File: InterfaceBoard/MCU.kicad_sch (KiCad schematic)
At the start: 1 part, among them J1 Conn_ARM_JTAG_SWD_10

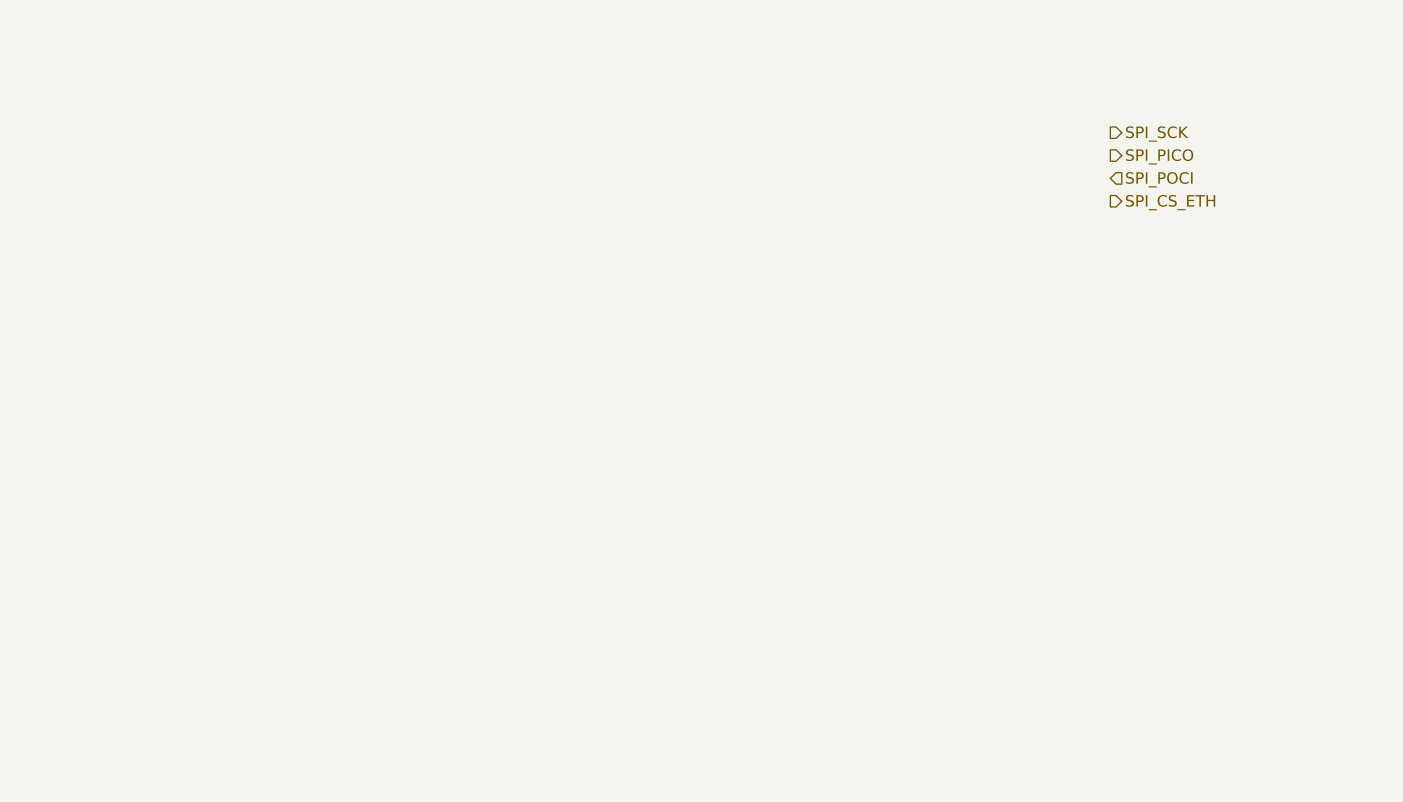
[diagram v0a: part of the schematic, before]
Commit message: InterfaceBoard: Add RS-232/DE-9
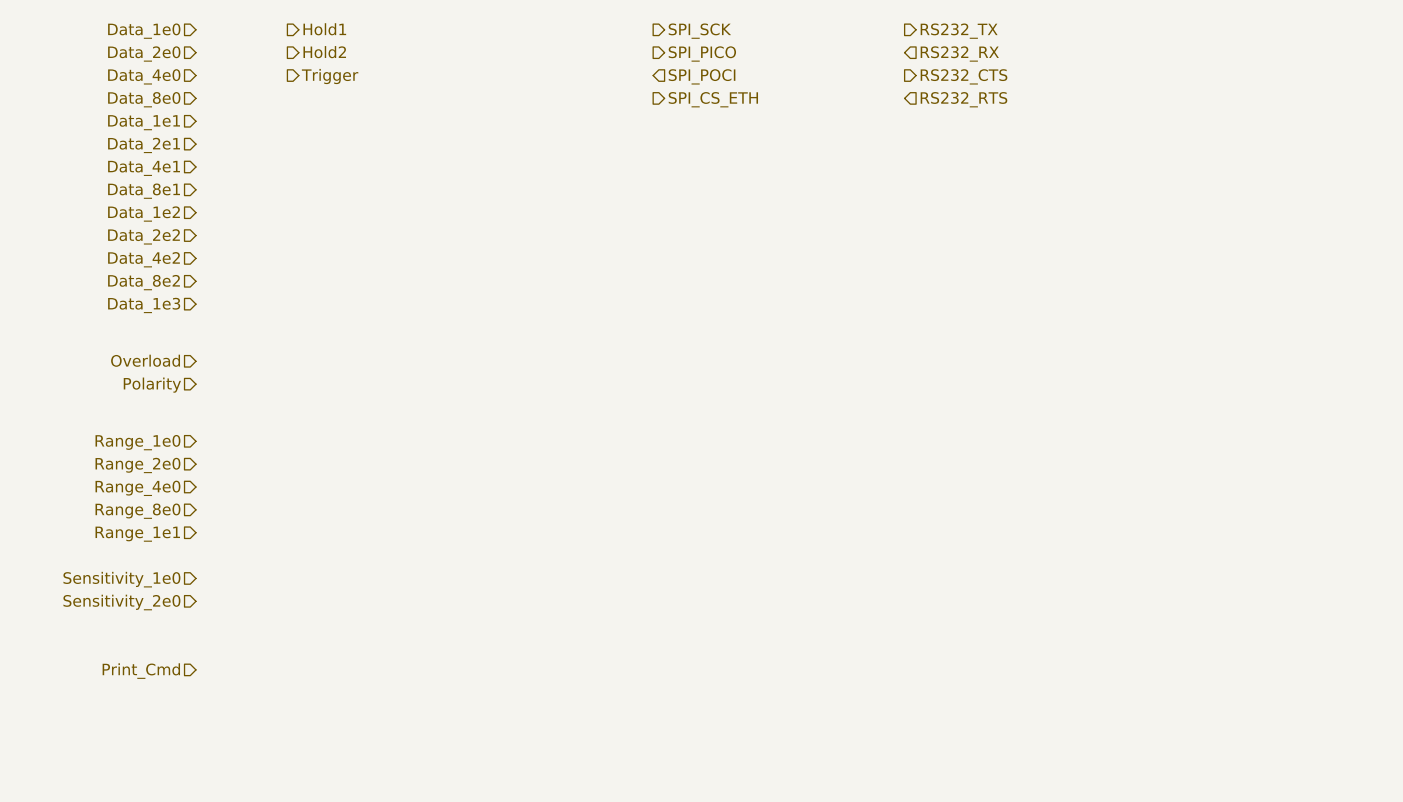
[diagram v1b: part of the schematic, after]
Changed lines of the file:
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@@
 (kicad_sch (version 20211123) (generator eeschema)
   (paper "A4")
-  (hierarchical_label "SPI_POCI" (shape input) (at 137.16 34.29 0)
+  (hierarchical_label "Data_2e0" (shape input) (at 35.56 20.32 180)
+    (effects (font (size 1.27 1.27)) (justify right))
+  )
+  (hierarchical_label "Hold1" (shape output) (at 45.72 17.78 0)
     (effects (font (size 1.27 1.27)) (justify left))
   )
-  (hierarchical_label "SPI_PICO" (shape output) (at 137.16 31.75 0)
+  (hierarchical_label "RS232_RTS" (shape input) (at 114.3 25.4 0)
     (effects (font (size 1.27 1.27)) (justify left))
   )
-  (hierarchical_label "SPI_CS_ETH" (shape output) (at 137.16 36.83 0)
+  (hierarchical_label "Range_4e0" (shape input) (at 35.56 68.58 180)
+    (effects (font (size 1.27 1.27)) (justify right))
+  )
+  (hierarchical_label "Data_1e1" (shape input) (at 35.56 27.94 180)
+    (effects (font (size 1.27 1.27)) (justify right))
+  )
+  (hierarchical_label "RS232_TX" (shape output) (at 114.3 17.78 0)
     (effects (font (size 1.27 1.27)) (justify left))
   )
-  (hierarchical_label "SPI_SCK" (shape output) (at 137.16 29.21 0)
+  (hierarchical_label "RS232_RX" (shape input) (at 114.3 20.32 0)
     (effects (font (size 1.27 1.27)) (justify left))
   )
+  (hierarchical_label "Print_Cmd" (shape input) (at 35.56 88.9 180)
+    (effects (font (size 1.27 1.27)) (justify right))
+  )
+  (hierarchical_label "Data_1e3" (shape input) (at 35.56 48.26 180)
+    (effects (font (size 1.27 1.27)) (justify right))
+  )
+  (hierarchical_label "Data_4e2" (shape input) (at 35.56 43.18 180)
+    (effects (font (size 1.27 1.27)) (justify right))
+  )
+  (hierarchical_label "Data_4e1" (shape input) (at 35.56 33.02 180)
+    (effects (font (size 1.27 1.27)) (justify right))
+  )
+  (hierarchical_label "Hold2" (shape output) (at 45.72 20.32 0)
+    (effects (font (size 1.27 1.27)) (justify left))
+  )
+  (hierarchical_label "Data_8e0" (shape input) (at 35.56 25.4 180)
+    (effects (font (size 1.27 1.27)) (justify right))
+  )
+  (hierarchical_label "Range_2e0" (shape input) (at 35.56 66.04 180)
+    (effects (font (size 1.27 1.27)) (justify right))
+  )
+  (hierarchical_label "Sensitivity_1e0" (shape input) (at 35.56 78.74 180)
+    (effects (font (size 1.27 1.27)) (justify right))
+  )
+  (hierarchical_label "SPI_POCI" (shape input) (at 86.36 22.86 0)
+    (effects (font (size 1.27 1.27)) (justify left))
+  )
+  (hierarchical_label "Data_8e1" (shape input) (at 35.56 35.56 180)
+    (effects (font (size 1.27 1.27)) (justify right))
+  )
+  (hierarchical_label "SPI_PICO" (shape output) (at 86.36 20.32 0)
+    (effects (font (size 1.27 1.27)) (justify left))
+  )
+  (hierarchical_label "Overload" (shape input) (at 35.56 54.61 180)
+    (effects (font (size 1.27 1.27)) (justify right))
+  )
+  (hierarchical_label "Range_1e1" (shape input) (at 35.56 73.66 180)
+    (effects (font (size 1.27 1.27)) (justify right))
+  )
+  (hierarchical_label "Data_1e0" (shape input) (at 35.56 17.78 180)
+    (effects (font (size 1.27 1.27)) (justify right))
+  )
+  (hierarchical_label "SPI_CS_ETH" (shape output) (at 86.36 25.4 0)
+    (effects (font (size 1.27 1.27)) (justify left))
+  )
+  (hierarchical_label "Range_8e0" (shape input) (at 35.56 71.12 180)
+    (effects (font (size 1.27 1.27)) (justify right))
+  )
+  (hierarchical_label "RS232_CTS" (shape output) (at 114.3 22.86 0)
+    (effects (font (size 1.27 1.27)) (justify left))
+  )
+  (hierarchical_label "Trigger" (shape output) (at 45.72 22.86 0)
+    (effects (font (size 1.27 1.27)) (justify left))
+  )
+  (hierarchical_label "Data_4e0" (shape input) (at 35.56 22.86 180)
+    (effects (font (size 1.27 1.27)) (justify right))
+  )
+  (hierarchical_label "Data_2e1" (shape input) (at 35.56 30.48 180)
+    (effects (font (size 1.27 1.27)) (justify right))
+  )
+  (hierarchical_label "SPI_SCK" (shape output) (at 86.36 17.78 0)
+    (effects (font (size 1.27 1.27)) (justify left))
+  )
+  (hierarchical_label "Range_1e0" (shape input) (at 35.56 63.5 180)
+    (effects (font (size 1.27 1.27)) (justify right))
+  )
+  (hierarchical_label "Data_2e2" (shape input) (at 35.56 40.64 180)
+    (effects (font (size 1.27 1.27)) (justify right))
+  )
+  (hierarchical_label "Sensitivity_2e0" (shape input) (at 35.56 81.28 180)
+    (effects (font (size 1.27 1.27)) (justify right))
+  )
+  (hierarchical_label "Data_8e2" (shape input) (at 35.56 45.72 180)
+    (effects (font (size 1.27 1.27)) (justify right))
+  )
+  (hierarchical_label "Polarity" (shape input) (at 35.56 57.15 180)
+    (effects (font (size 1.27 1.27)) (justify right))
+  )
+  (hierarchical_label "Data_1e2" (shape input) (at 35.56 38.1 180)
+    (effects (font (size 1.27 1.27)) (justify right))
+  )
   (symbol (lib_id "Connector:Conn_ARM_JTAG_SWD_10") (at 232.41 86.36 0) (unit 1)

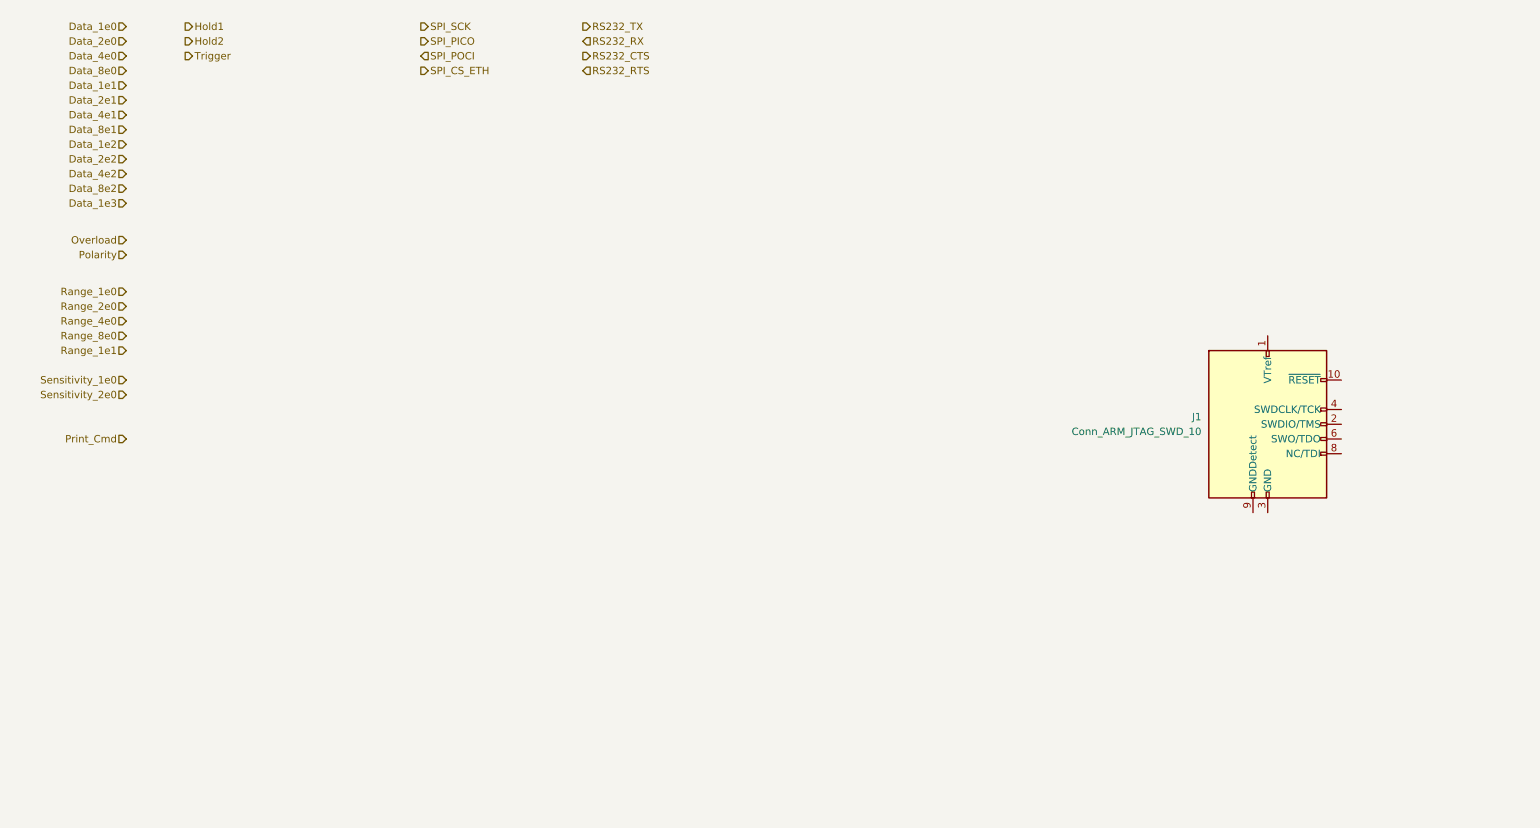
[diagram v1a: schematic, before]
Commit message: InterfaceBoard: Add STM32G0B1RET
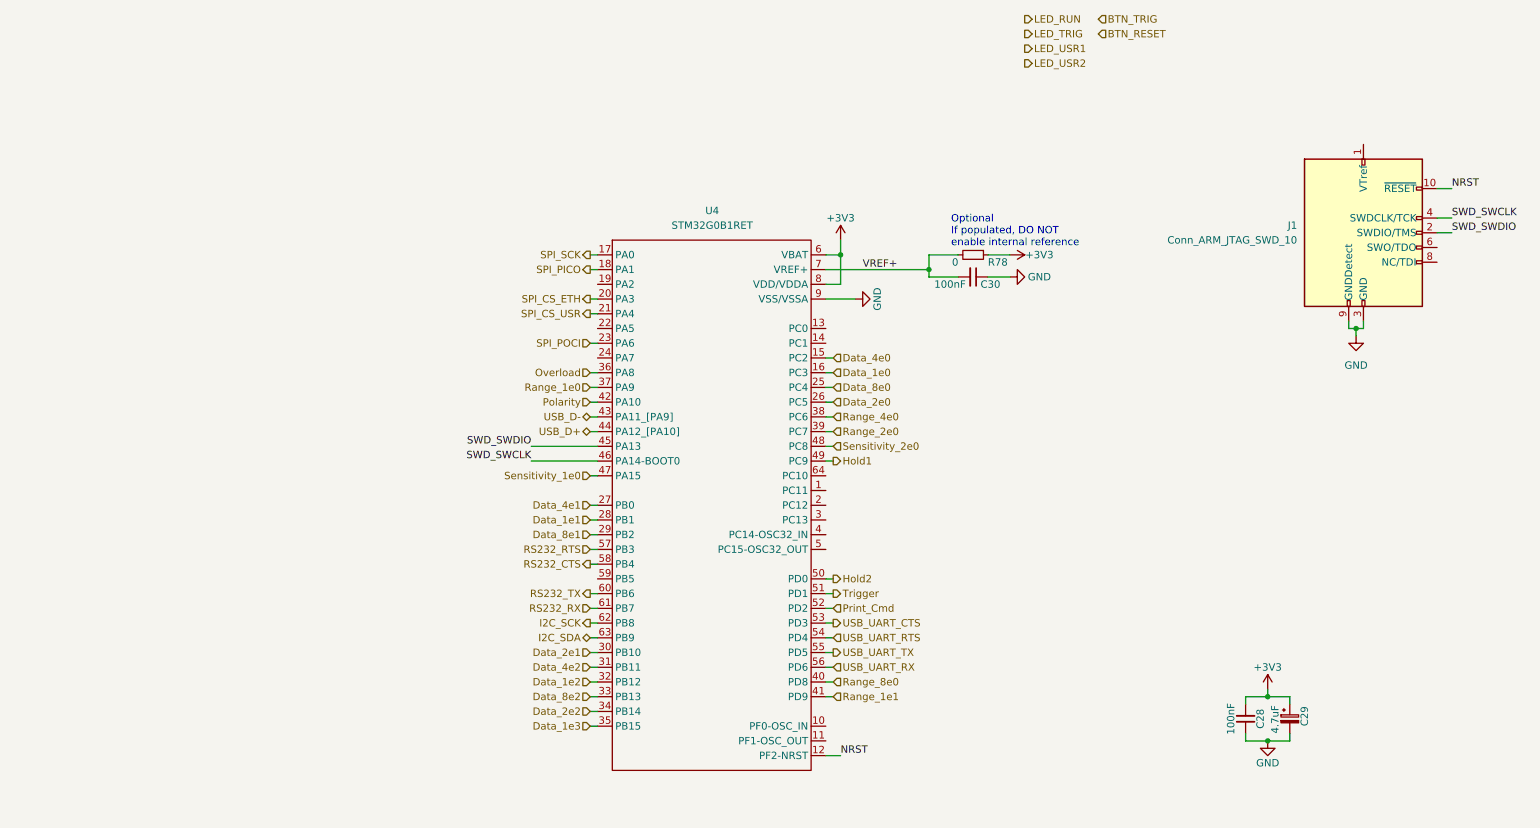
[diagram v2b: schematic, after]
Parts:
- added C28, C30: 100nF, Capacitor_SMD:C_0603_1608Metric, symbol Device:C_Small
- added C29: 4.7uF, Capacitor_SMD:CP_Elec_5x5.9, symbol Device:C_Polarized_Small
- added R78: 0, Resistor_SMD:R_0603_1608Metric, symbol Device:R_Small
- added U4: STM32G0B1RET, Package_QFP:LQFP-64_10x10mm_P0.5mm, symbol lib_symbols:STM32G0B1RET
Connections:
- net Data_1e0: now also U4.16 (PC3)
- net Data_1e1: now also U4.28 (PB1)
- net Data_1e2: now also U4.32 (PB12)
- net Data_1e3: now also U4.35 (PB15)
- net Data_2e0: now also U4.26 (PC5)
- net Data_2e1: now also U4.30 (PB10)
- net Data_2e2: now also U4.34 (PB14)
- net Data_4e0: now also U4.15 (PC2)
- net Data_4e1: now also U4.27 (PB0)
- net Data_4e2: now also U4.31 (PB11)
- net Data_8e0: now also U4.25 (PC4)
- net Data_8e1: now also U4.29 (PB2)
- net Data_8e2: now also U4.33 (PB13)
- net Hold1: now also U4.49 (PC9)
- net Hold2: now also U4.50 (PD0)
- net Overload: now also U4.36 (PA8)
- net Polarity: now also U4.42 (PA10)
- net Print_Cmd: now also U4.52 (PD2)
- net RS232_CTS: now also U4.58 (PB4)
- net RS232_RTS: now also U4.57 (PB3)
- net RS232_RX: now also U4.61 (PB7)
- net RS232_TX: now also U4.60 (PB6)
- net Range_1e0: now also U4.37 (PA9)
- net Range_1e1: now also U4.41 (PD9)
- net Range_2e0: now also U4.39 (PC7)
- net Range_4e0: now also U4.38 (PC6)
- net Range_8e0: now also U4.40 (PD8)
- net SPI_CS_ETH: now also U4.20 (PA3)
- net SPI_PICO: now also U4.18 (PA1)
- net SPI_POCI: now also U4.23 (PA6)
- net SPI_SCK: now also U4.17 (PA0)
- net Sensitivity_1e0: now also U4.47 (PA15)
- net Sensitivity_2e0: now also U4.48 (PC8)
- net Trigger: now also U4.51 (PD1)
- net NRST: now reaches J1.10 (~{RESET})
- net NRST: now also U4.12 (PF2-NRST)
- net SWD_SWDIO: now reaches J1.2 (SWDIO/TMS)
- net SWD_SWDIO: now also U4.45 (PA13)
- net GND: now reaches J1.3 (GND), J1.5 (GND)
- net GND: now also J1.9 (GNDDetect), C28.1, C29.2, C30.1, U4.9 (VSS/VSSA)
- net SWD_SWCLK: now reaches J1.4 (SWDCLK/TCK)
- net SWD_SWCLK: now also U4.46 (PA14-BOOT0)
- new net +3V3: C28.2, C29.1, R78.1, U4.6 (VBAT), U4.8 (VDD/VDDA)
- new net I2C_SCK: U4.62 (PB8)
- new net I2C_SDA: U4.63 (PB9)
- new net SPI_CS_USR: U4.21 (PA4)
- new net USB_D+: U4.44 (PA12_[PA10])
- new net USB_D-: U4.43 (PA11_[PA9])
- new net USB_UART_CTS: U4.53 (PD3)
- new net USB_UART_RTS: U4.54 (PD4)
- new net USB_UART_RX: U4.56 (PD6)
- new net USB_UART_TX: U4.55 (PD5)
- new net VREF+: C30.2, R78.2, U4.7 (VREF+)
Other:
- note added: "Optional If populated, DO NOT enable internal reference"
- moved on the sheet: J1

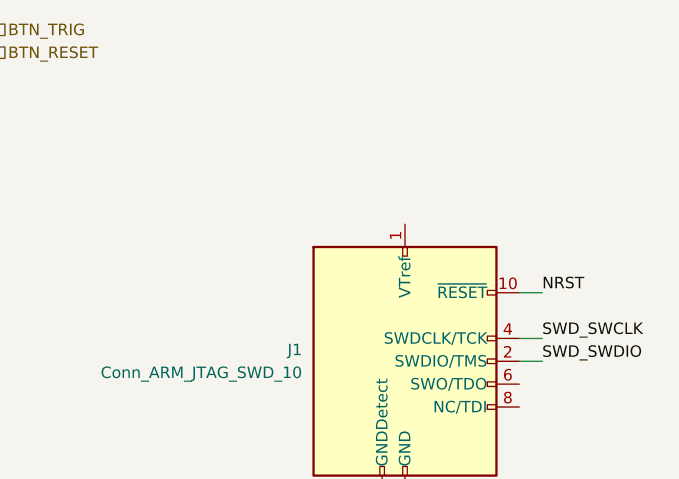
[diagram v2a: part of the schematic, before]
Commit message: InterfaceBoard: Make library paths relative
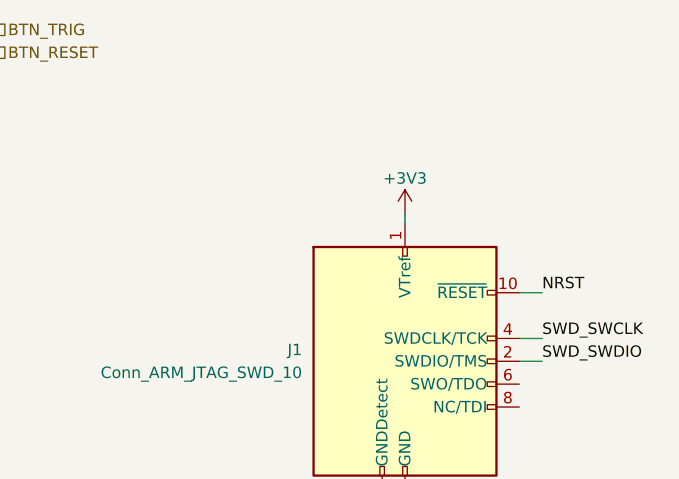
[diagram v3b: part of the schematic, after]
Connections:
- net +3V3: now also J1.1 (VTref)
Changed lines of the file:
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@@
+    (stroke (width 0) (type default) (color 0 0 0 0))
+  )
+  (wire (pts (xy 248.92 36.83) (xy 248.92 38.1))
     (stroke (width 0) (type default) (color 0 0 0 0))
   )
@@
     (pin "2")
   )
+  (symbol (lib_id "power:+3V3") (at 248.92 36.83 0) (unit 1)
+    (in_bom yes) (on_board yes)
+    (property "Reference" "#PWR?" (id 0) (at 248.92 40.64 0)
+      (effects (font (size 1.27 1.27)) hide)
+    )
+    (property "Value" "+3V3" (id 1) (at 248.92 33.02 0))
+    (property "Footprint" "" (id 2) (at 248.92 36.83 0)
+      (effects (font (size 1.27 1.27)) hide)
+    )
+    (property "Datasheet" "" (id 3) (at 248.92 36.83 0)
+      (effects (font (size 1.27 1.27)) hide)
+    )
+    (pin "1")
+  )
   (symbol (lib_id "lib_symbols:STM32G0B1RET") (at 137.16 54.61 0) (unit 1)
